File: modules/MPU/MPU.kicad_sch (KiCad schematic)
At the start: 17 parts, among them J1 CardConnector, U1 74HCT541, U3 W65C02, U4 74HCT541, U5 74HCT10, U6 74HCT245N, U7 74HCT541, U8 74HCT541, Y1 1Mhz

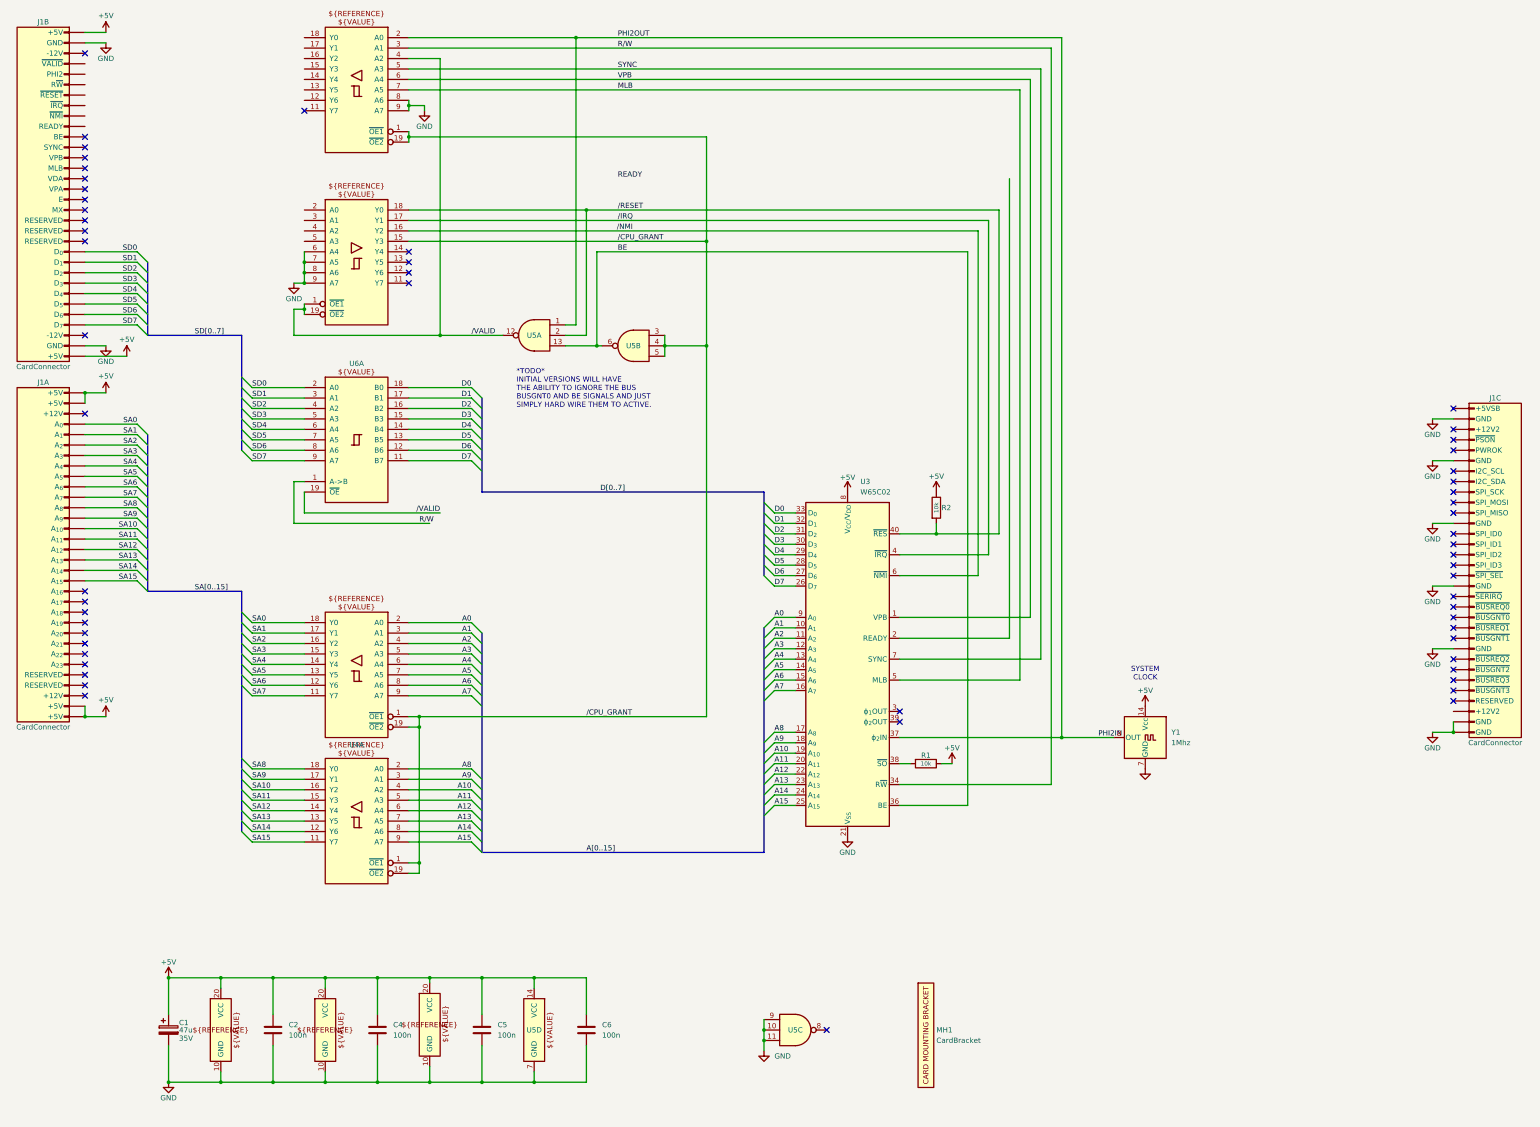
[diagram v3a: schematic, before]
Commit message: migrated PWR to SCC; updates to MPU, more work pending
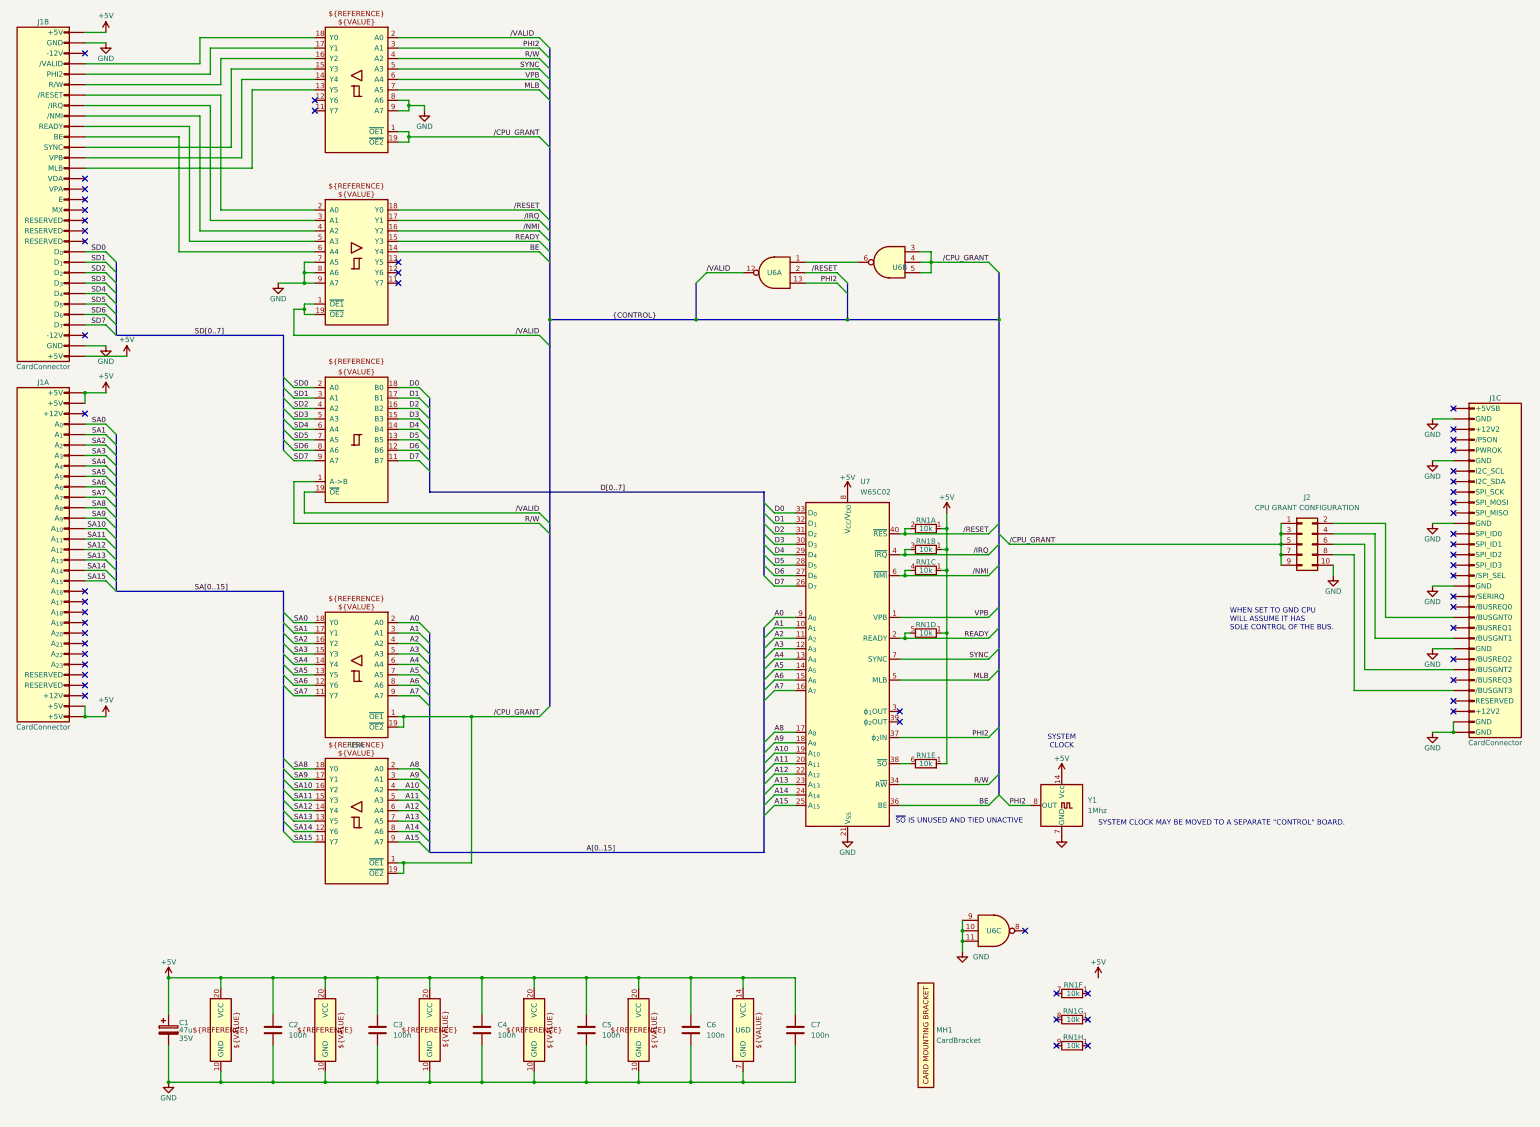
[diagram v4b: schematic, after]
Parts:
- removed R1, R2: 10k, IMNOTWOPR:R_Axial_DIN0207_P400mil, symbol IMNOTWOPR:R
- removed unit 2 of U1
- removed unit 2 of U4
- removed unit 4 of U5
- removed unit 2 of U6
- added C6, C7: 100n, FormantKO:C_Rect_P200mil, symbol FormantKO:C
- added J2: CPU GRANT CONFIGURATION, Connector_PinHeader_2.54mm:PinHeader_2x05_P2.54mm_Vertical, symbol Connector_Generic:Conn_02x05_Odd_Even
- added RN1: 10k, Resistor_THT:R_Array_SIP9, symbol Device:R_Network08_Split
- added unit 1 of U1
- added unit 1 of U2
- added unit 1 of U3
- added unit 1 of U4
- added unit 1 of U5
- added unit 4 of U6
- U1: renamed from U7; value 74HCT541 -> 74AHCT541; symbol IMNOTWOPR:74HCT541 -> IMNOTWOPR:74AHCT541
- U2: renamed from U8; value 74HCT541 -> 74AHCT541; symbol IMNOTWOPR:74HCT541 -> IMNOTWOPR:74AHCT541
- U3: renamed from U6; value 74HCT245N -> 74AHCT245; symbol IMNOTWOPR:74HCT245 -> IMNOTWOPR:74AHCT245
- U4: renamed from U1; value 74HCT541 -> 74AHCT541; symbol IMNOTWOPR:74HCT541 -> IMNOTWOPR:74AHCT541
- U5: renamed from U4; value 74HCT541 -> 74AHCT541; symbol IMNOTWOPR:74HCT541 -> IMNOTWOPR:74AHCT541
- U6: renamed from U5; footprint (none) -> IMNOTWOPR:DIP-14N
- renumbered C4 to C3, C5 to C4, C6 to C5, U3 to U7
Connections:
- net +5V: now also U1.20 (VCC), U2.20 (VCC), U3.20 (VCC), U4.20 (VCC), U5.20 (VCC), C6.1, C7.1, RN1.1 (R1), RN1.1 (R1), RN1.1 (R1), RN1.1 (R1), RN1.1 (R1), U6.14 (VCC)
- net A0: now also U4.2 (A0); no longer U4.2 (A0)
- net A1: now also U4.3 (A1); no longer U4.3 (A1)
- net A10: now also U5.4 (A2); no longer U5.4 (A2)
- net A11: now also U5.5 (A3); no longer U5.5 (A3)
- net A12: now also U5.6 (A4); no longer U5.6 (A4)
- net A13: now also U5.7 (A5); no longer U5.7 (A5)
- net A14: now also U5.8 (A6); no longer U5.8 (A6)
- net A15: now also U5.9 (A7); no longer U5.9 (A7)
- net A2: now also U4.4 (A2); no longer U4.4 (A2)
- net A3: now also U4.5 (A3); no longer U4.5 (A3)
- net A4: now also U4.6 (A4); no longer U4.6 (A4)
- net A5: now also U4.7 (A5); no longer U4.7 (A5)
- net A6: now also U4.8 (A6); no longer U4.8 (A6)
- net A7: now also U4.9 (A7); no longer U4.9 (A7)
- net A8: now also U5.2 (A0); no longer U5.2 (A0)
- net A9: now also U5.3 (A1); no longer U5.3 (A1)
- net BE: now also U2.14 (Y4); no longer U6.13, U6.6
- net D0: now also U3.18 (B0); no longer U3.18 (B0)
- net D1: now also U3.17 (B1); no longer U3.17 (B1)
- net D2: now also U3.16 (B2); no longer U3.16 (B2)
- net D3: now also U3.15 (B3); no longer U3.15 (B3)
- net D4: now also U3.14 (B4); no longer U3.14 (B4)
- net D5: now also U3.13 (B5); no longer U3.13 (B5)
- net D6: now also U3.12 (B6); no longer U3.12 (B6)
- net D7: now also U3.11 (B7); no longer U3.11 (B7)
- net GND: now also U1.10 (GND), U2.10 (GND), U3.10 (GND), U4.10 (GND), U5.10 (GND), C6.2, C7.2, J2.10 (Pin_10), U1.8 (A6), U1.9 (A7), U2.7 (A5), U2.8 (A6), U2.9 (A7), U6.7 (GND); no longer U1.8 (A6), U1.9 (A7), U2.6 (A4), U2.7 (A5), U2.8 (A6), U2.9 (A7)
- net MLB: now also U1.7 (A5); no longer U1.7 (A5)
- net READY: now also U7.2 (READY), RN1.5 (R4.2), U2.15 (Y3)
- net R/W: now also U1.4 (A2), U3.1 (A->B); no longer U1.3 (A1), U3.1 (A->B)
- net SA0: now also U4.18 (Y0); no longer U4.18 (Y0)
- net SA1: now also U4.17 (Y1); no longer U4.17 (Y1)
- net SA10: now also U5.16 (Y2); no longer U5.16 (Y2)
- net SA11: now also U5.15 (Y3); no longer U5.15 (Y3)
- net SA12: now also U5.14 (Y4); no longer U5.14 (Y4)
- net SA13: now also U5.13 (Y5); no longer U5.13 (Y5)
- net SA14: now also U5.12 (Y6); no longer U5.12 (Y6)
- net SA15: now also U5.11 (Y7); no longer U5.11 (Y7)
- net SA2: now also U4.16 (Y2); no longer U4.16 (Y2)
- net SA3: now also U4.15 (Y3); no longer U4.15 (Y3)
- net SA4: now also U4.14 (Y4); no longer U4.14 (Y4)
- net SA5: now also U4.13 (Y5); no longer U4.13 (Y5)
- net SA6: now also U4.12 (Y6); no longer U4.12 (Y6)
- net SA7: now also U4.11 (Y7); no longer U4.11 (Y7)
- net SA8: now also U5.18 (Y0); no longer U5.18 (Y0)
- net SA9: now also U5.17 (Y1); no longer U5.17 (Y1)
- net SD0: now also U3.2 (A0); no longer U3.2 (A0)
- net SD1: now also U3.3 (A1); no longer U3.3 (A1)
- net SD2: now also U3.4 (A2); no longer U3.4 (A2)
- net SD3: now also U3.5 (A3); no longer U3.5 (A3)
- net SD4: now also U3.6 (A4); no longer U3.6 (A4)
- net SD5: now also U3.7 (A5); no longer U3.7 (A5)
- net SD6: now also U3.8 (A6); no longer U3.8 (A6)
- net SD7: now also U3.9 (A7); no longer U3.9 (A7)
- net SYNC: now also U1.5 (A3); no longer U1.5 (A3)
- net VPB: now also U1.6 (A4); no longer U1.6 (A4)
- net /CPU_GRANT: now also J2.1 (Pin_1), J2.3 (Pin_3), J2.5 (Pin_5), J2.7 (Pin_7), J2.9 (Pin_9), U1.1 (~{OE1}), U1.19 (~{OE2}), U4.1 (~{OE1}), U4.19 (~{OE2}), U5.1 (~{OE1}), U5.19 (~{OE2}); no longer U1.1 (~{OE1}), U1.19 (~{OE2}), U2.15 (Y3), U4.1 (~{OE1}), U4.19 (~{OE2}), U5.1 (~{OE1}), U5.19 (~{OE2})
- net /IRQ: now also RN1.3 (R2.2), U2.17 (Y1); no longer U2.17 (Y1)
- net /NMI: now also RN1.4 (R3.2), U2.16 (Y2); no longer U2.16 (Y2)
- net /RESET: now also RN1.2 (R1.2), U2.18 (Y0); no longer U2.18 (Y0)
- net /VALID: now also U1.2 (A0), U2.1 (~{OE1}), U2.19 (~{OE2}), U3.19 (~{OE}); no longer U1.4 (A2), U2.1 (~{OE1}), U2.19 (~{OE2}), U3.19 (~{OE})
- net at U7.38 (~{SO}): now also RN1.6 (R5.2)
- net at J1.c21 (/BUSGNT0): now also J2.2 (Pin_2)
- net at J1.c23 (/BUSGNT1): now also J2.4 (Pin_4)
- net at J1.c26 (/BUSGNT2): now also J2.6 (Pin_6)
- net at J1.c28 (/BUSGNT3): now also J2.8 (Pin_8)
- net at J1.b10 (READY): now also U2.5 (A3)
- net at J1.b11 (BE): now also U2.6 (A4)
- net at J1.b12 (SYNC): now also U1.15 (Y3)
- net at J1.b13 (VPB): now also U1.14 (Y4)
- net at J1.b14 (MLB): now also U1.13 (Y5)
- net at J1.b4 (/VALID): now also U1.18 (Y0)
- net at J1.b5 (PHI2): now also U1.17 (Y1)
- net at J1.b6 (R/W): now also U1.16 (Y2)
- net at J1.b7 (/RESET): now also U2.2 (A0)
- net at J1.b8 (/IRQ): now also U2.3 (A1)
- net at J1.b9 (/NMI): now also U2.4 (A2)
- net PHI2IN renamed PHI2
- net PHI2: now also U6.13, U1.3 (A1); no longer U1.2 (A0), U6.1
- new net: U6.1, U6.6
- no-connect marks 57 -> 56
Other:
- note added: "SYSTEM CLOCK MAY BE MOVED TO A SEPARATE "CONTROL" BOARD."
- note added: "WHEN SET TO GND CPU WILL ASSUME IT HAS SOLE CONTROL OF THE BUS."
- note added: "~{SO} IS UNUSED AND TIED UNACTIVE"
- note removed: "*TODO* INITIAL VERSIONS WILL HAVE THE ABILITY TO IGNORE THE BUS BUSGNT0 AND BE SIGNALS AND JUST SIMPLY HARD WIRE THEM TO ACTIVE."
- moved on the sheet: J1C, U6A, U6B, U6C, Y1
